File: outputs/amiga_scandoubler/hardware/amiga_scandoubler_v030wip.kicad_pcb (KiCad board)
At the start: 4 copper layers, 95 x 95 mm, 135 parts, among them J1 33DSMT1-E15SNCT, J2 33DSMT1-E15SNCT, J3 TYPE-C-31-M-12, J4 JTAG 2x05 2.54mm, U1 TVP7002PZP, U2 GW1N-LV4QN88C6/I5, U3 ADV7125KSTZ140, U4 SN74LVC2G17DBVR, U5 SN74LVC2G17DBVR, U6 SN74LVC1G17DBVR, U7 TPS62160DSGR, U8 TPS62160DSGR, U9 TPS62160DSGR, Y1 27MHz ECS-3225MVLC

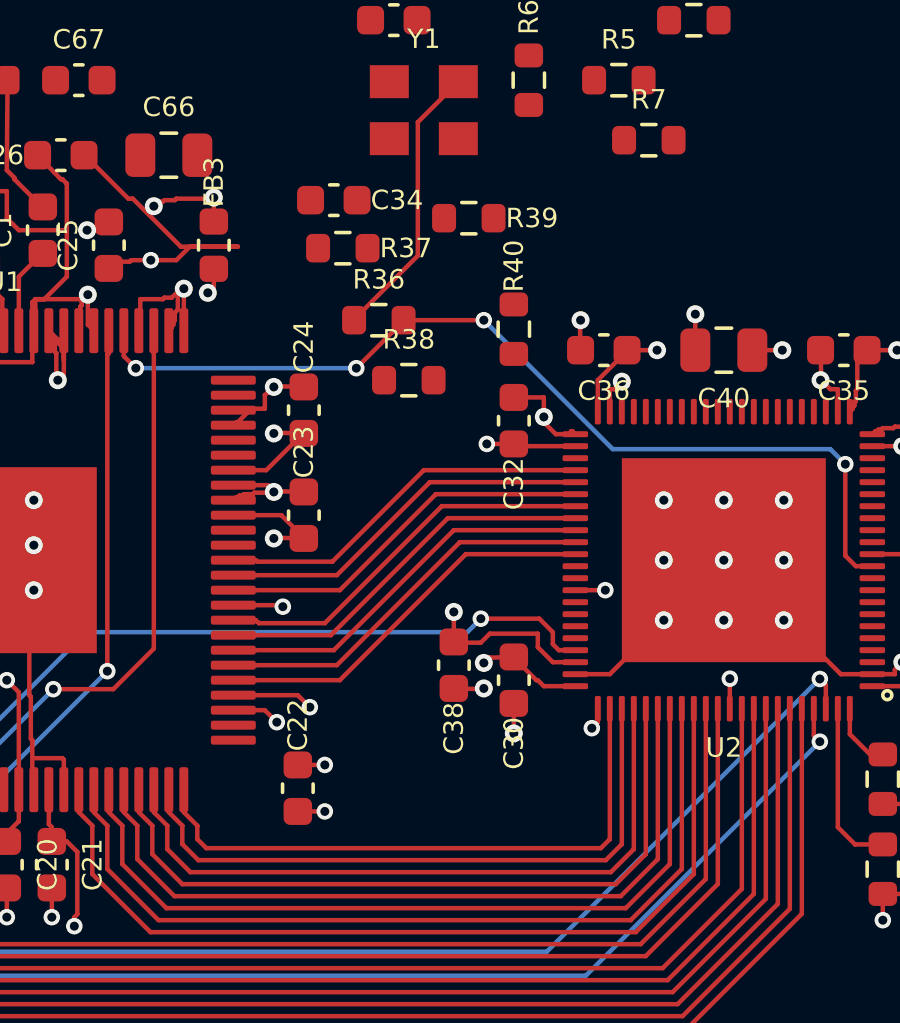
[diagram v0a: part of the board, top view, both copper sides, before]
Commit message: v030wip: C34(U2 3V3 パスコン)の孤立を解消
- C34 を (37,30) から U2 左下角 (45.4,49.15, 270°) へ移動
- pad1(3V3) を U2.67 の既存 3V3 ビアへ接続、pad2(GND) に GND ビアを追加
- U2 左の制御線予約領域と B.Cu 通路は回避
- KiCad 7 DRC: エラー 0、未接続 112→110 (3V3/GND 各 -1 のみ)
- 電源監査: 電源 75・GND 80 件 PASS。残る FAIL は U2 再ピン由来(課題5/9)
- CLAUDE.md と revision_0.30wip.md を更新、配置スクリプトを追加

Co-Authored-By: Claude Opus 5.5 <noreply@anthropic.com>
Claude-Session: https://claude.ai/code/session_019f929sAJ7LRnJRRFvA6g9F
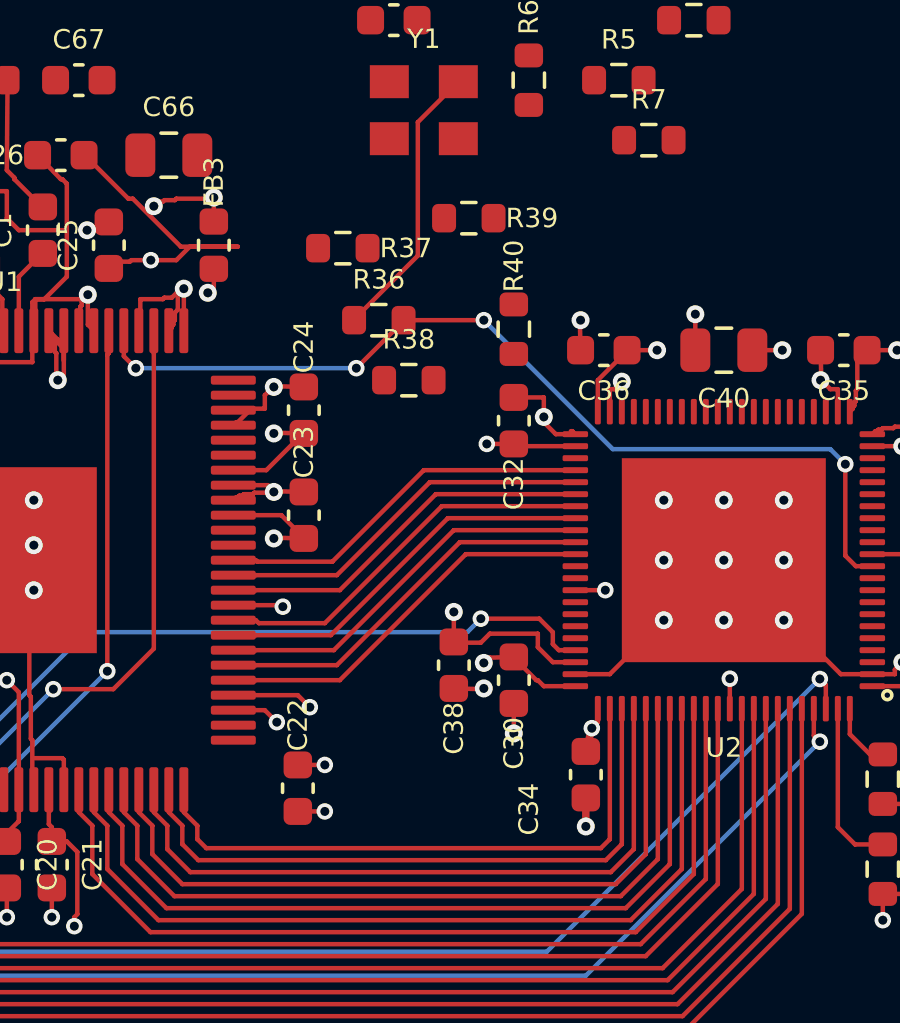
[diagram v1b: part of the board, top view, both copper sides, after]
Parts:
- moved C34 20.9 mm to (45.4, 49.1), turned to -90 degrees
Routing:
- net GND: track 349.1 -> 350.0 mm, vias 102 -> 103
- net 3V3: track 77.3 -> 78.1 mm
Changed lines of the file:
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@@
   )
   (footprint "Capacitor_SMD:C_0603_1608Metric" (layer "F.Cu")
-    (at 37 30)
+    (at 45.4 49.15 -90)
     (descr "Capacitor SMD 0603 (1608 Metric), square (rectangular) end terminal, IPC_7351 nominal, (Body size source: IPC-SM-782 page 76, https://www.pcb-3d.com/wordpress/wp-content/uploads/ipc-sm-782a_amendment_1_and_2.pdf), generated with kicad-footprint-generator")
     (tags "capacitor")
     (attr smd)
-    (fp_text reference "C34" (at 2.105001 0) (layer "F.SilkS")
+    (fp_text reference "C34" (at 1.15 1.9 -90) (layer "F.SilkS")
         (effects (font (size 0.65 0.65) (thickness 0.1)))
     )
-    (fp_text value "100nF" (at 0 1.43) (layer "F.Fab") hide
+    (fp_text value "100nF" (at 0 1.43 -90) (layer "F.Fab") hide
         (effects (font (size 1 1) (thickness 0.15)))
     )
-    (fp_text user "${REFERENCE}" (at 0 0) (layer "F.Fab")
+    (fp_text user "${REFERENCE}" (at 0 0 -90) (layer "F.Fab")
         (effects (font (size 0.4 0.4) (thickness 0.06)))
     )
@@
     (fp_line (start 0.8 0.4) (end -0.8 0.4)
       (stroke (width 0.1) (type solid)) (layer "F.Fab"))
-    (pad "1" smd roundrect (at -0.775 0) (size 0.9 0.95) (layers "F.Cu" "F.Paste" "F.Mask") (roundrect_rratio 0.25)
+    (pad "1" smd roundrect (at -0.775 0 270) (size 0.9 0.95) (layers "F.Cu" "F.Paste" "F.Mask") (roundrect_rratio 0.25)
       (net 54 "3V3"))
-    (pad "2" smd roundrect (at 0.775 0) (size 0.9 0.95) (layers "F.Cu" "F.Paste" "F.Mask") (roundrect_rratio 0.25)
+    (pad "2" smd roundrect (at 0.775 0 270) (size 0.9 0.95) (layers "F.Cu" "F.Paste" "F.Mask") (roundrect_rratio 0.25)
       (net 43 "GND"))
     (model "${KICAD6_3DMODEL_DIR}/Capacitor_SMD.3dshapes/C_0603_1608Metric.wrl"
@@
   (segment (start 75.4 37.55) (end 75.45 37.5) (width 0.15) (layer "F.Cu") (net 43))
   (segment (start 43 47.8) (end 43 47.775) (width 0.15) (layer "F.Cu") (net 43))
+  (segment (start 45.4 49.925) (end 45.4 50.875) (width 0.25) (layer "F.Cu") (net 43))
   (segment (start 16 40.225) (end 15.2 40.2) (width 0.15) (layer "F.Cu") (net 43))
   (segment (start 45.05 38.2) (end 43.3 38.2) (width 0.15) (layer "F.Cu") (net 43))
@@
   (via (at 16.95 36.8) (size 0.6) (drill 0.3) (layers "F.Cu" "B.Cu") (net 43))
   (via (at 28.8 33.15) (size 0.6) (drill 0.3) (layers "F.Cu" "B.Cu") (net 43))
+  (via (at 45.4 50.875) (size 0.6) (drill 0.3) (layers "F.Cu" "B.Cu") (net 43))
   (via (at 68.6375 44.95) (size 0.6) (drill 0.3) (layers "F.Cu" "B.Cu") (net 43))
   (via (at 15 40.425) (size 0.6) (drill 0.3) (layers "F.Cu" "B.Cu") (net 43))
@@
   (segment (start 27.6 50.9) (end 27.6 51.375) (width 0.15) (layer "F.Cu") (net 54))
   (segment (start 28.45 51.725) (end 28.45 53.8) (width 0.15) (layer "F.Cu") (net 54))
+  (segment (start 45.4 48.375) (end 45.6 47.6) (width 0.25) (layer "F.Cu") (net 54))
   (segment (start 54.35 36.85) (end 54.35 36.75) (width 0.15) (layer "F.Cu") (net 54))
   (segment (start 54.95 41.8) (end 56.45 41.8) (width 0.15) (layer "F.Cu") (net 54))

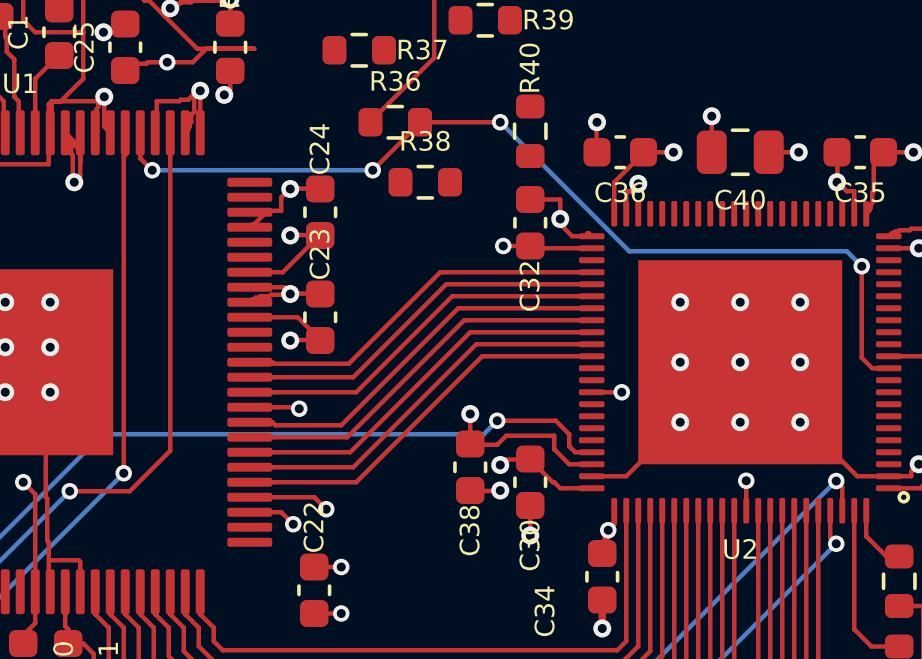
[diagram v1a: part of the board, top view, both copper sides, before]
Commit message: v030wip: 課題2 U2 左の制御線(SDA/SCL/RESET/PWDN)の本線を配線
- U1 内周ビア → B.Cu → U2 前面ビアで 4 本を接続(交差なし、各ビア2個)
  x=35 のビア列の隙間を上帯 SDA/SCL、下帯 RESET/PWDN で通過
- ADC_CLK の B.Cu 終点を (43.95,45.0) へ移し U2.60/61 の引き出し通路を確保
- U2.64 3V3 を内周ビアへ、U2.65 GND スタブを短縮
- KiCad 7 DRC: エラー 0、未接続 110→106(4ネット各 -1)。導通確認済み
- 電源監査: 電源 75・GND 80 PASS
- プルアップ R37–R40 は 0603 では収まらず未接続(判断待ち)
- KiCad 7 用編集ヘルパ pcbk7.py、配置探索 pullsearch.py、再現スクリプトを追加

Co-Authored-By: Claude Opus 5.5 <noreply@anthropic.com>
Claude-Session: https://claude.ai/code/session_019f929sAJ7LRnJRRFvA6g9F
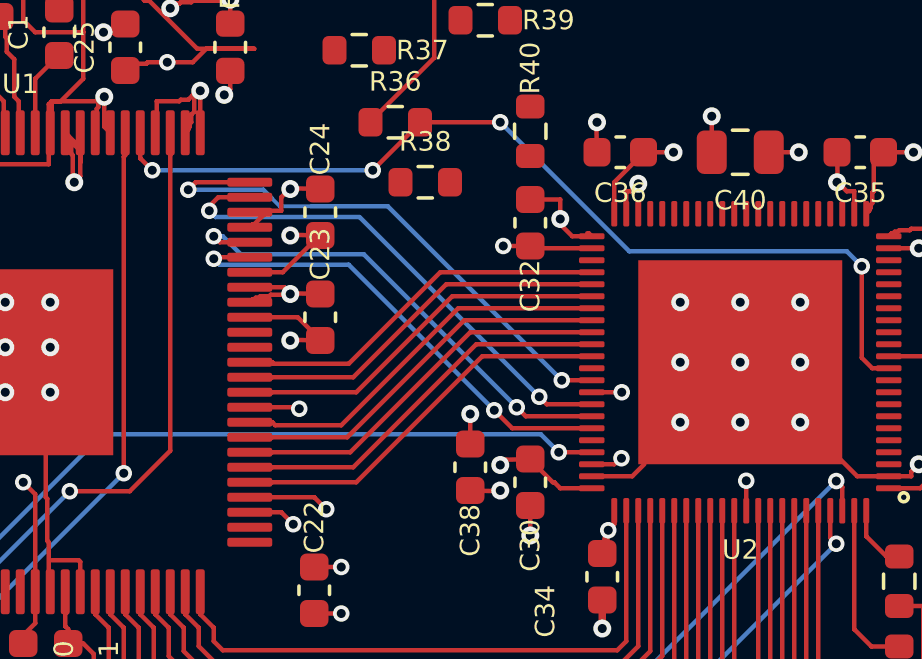
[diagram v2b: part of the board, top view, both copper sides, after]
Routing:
- net I2C_SDA: track 0.00 -> 18.2 mm, vias 0 -> 2
- net I2C_SCL: track 0.00 -> 17.0 mm, vias 0 -> 2
- net ADC_RESET_N: track 0.00 -> 16.4 mm, vias 0 -> 2
- net ADC_PWDN: track 0.00 -> 16.2 mm, vias 0 -> 2
- net GND: track 350.0 -> 345.4 mm
- net 3V3: track 78.1 -> 74.3 mm, vias 26 -> 27
- net ADC_CLK: track 28.9 -> 28.3 mm

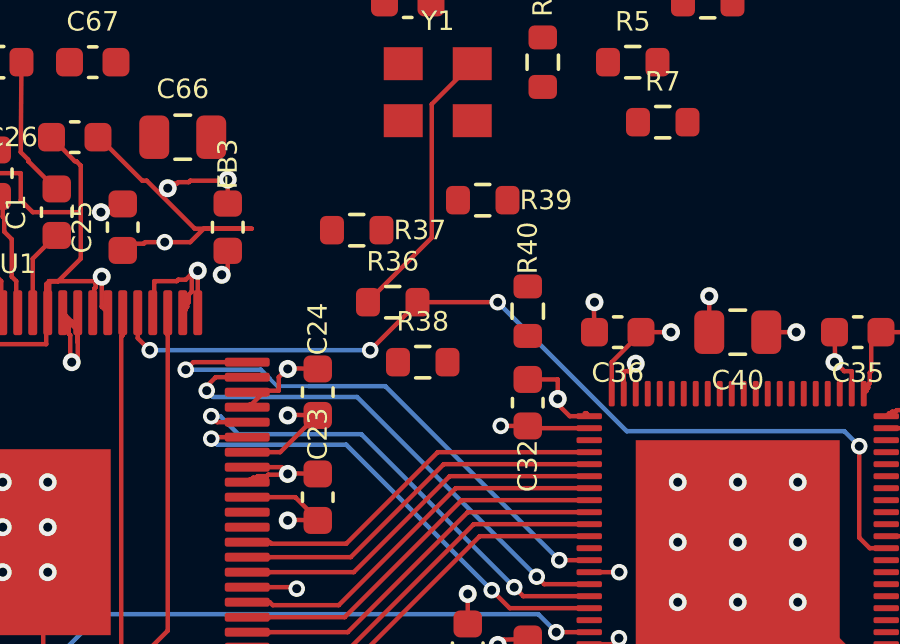
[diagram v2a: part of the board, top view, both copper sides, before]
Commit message: v030wip: R37–R40 を 0402 化してプルアップ／プルダウンを接続(課題2完了)
- 0603 では空き領域に収まらないため、利用者判断で R_0402_1005Metric に変更
- 4 本を縦置き 0.95mm ピッチで配置し、信号ビアを各 B.Cu 配線上へ
- 3V3/GND は面へのビア(R37 は R38 の 3V3 ビアを共用)
- 回路図・ネットリスト・circuit_manifest のフットプリント欄を更新
- KiCad 7 DRC: エラー 0、未接続 106→98。導通確認済み、電源監査 PASS

Co-Authored-By: Claude Opus 5.5 <noreply@anthropic.com>
Claude-Session: https://claude.ai/code/session_019f929sAJ7LRnJRRFvA6g9F
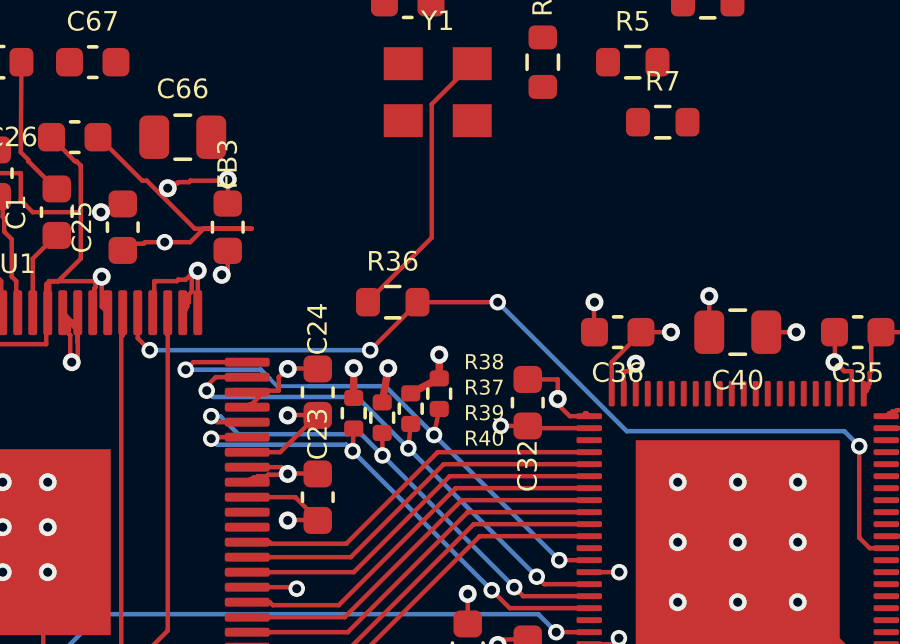
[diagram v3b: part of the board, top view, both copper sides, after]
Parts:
- R37, R38, R39, R40: footprint Resistor_SMD:R_0603_1608Metric -> R_0402_1005Metric
- moved R39 7.99 mm to (38.1, 37.9), turned to 90 degrees
- moved R40 6.72 mm to (37.2, 37.7)
- moved R37 6.22 mm to (39.1, 37.5), turned to 90 degrees
- moved R38 1.19 mm to (40.0, 37.0), turned to 90 degrees
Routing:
- net 3V3: track 74.3 -> 77.2 mm, vias 27 -> 29
- net GND: track 345.4 -> 346.6 mm, vias 103 -> 104
- net I2C_SDA: track 18.2 -> 19.1 mm, vias 2 -> 3
- net I2C_SCL: track 17.0 -> 17.9 mm, vias 2 -> 3
- net ADC_PWDN: track 16.2 -> 16.9 mm, vias 2 -> 3
- net ADC_RESET_N: track 16.4 -> 17.1 mm, vias 2 -> 3

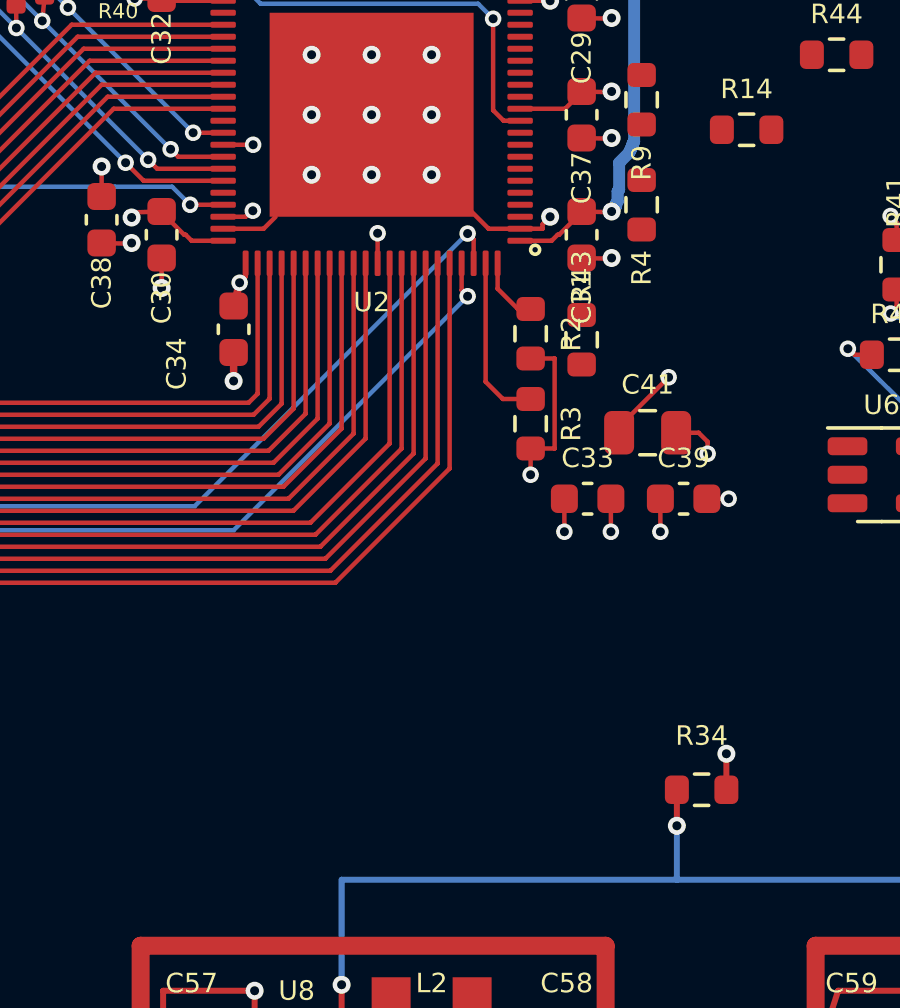
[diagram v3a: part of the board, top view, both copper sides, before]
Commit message: v030wip: 課題3 POWER_GOOD(U2.62)を既存の南側配線へ接続
- U2.62 → 内周ビア (46.04,44.45) → B.Cu で EP 下 y=44.65 を東へ
  → 45° で南東 → x=59.075 を南下 → 既存ビア (60.175,65.7)
- y=41 の通路は課題4(PSAVE)用に予約して回避
- KiCad 7 DRC: エラー 0、未接続 98→97(POWER_GOOD のみ)
- U8.8/U9.8/R34.1 との導通確認、電源監査 PASS

Co-Authored-By: Claude Opus 5.5 <noreply@anthropic.com>
Claude-Session: https://claude.ai/code/session_019f929sAJ7LRnJRRFvA6g9F
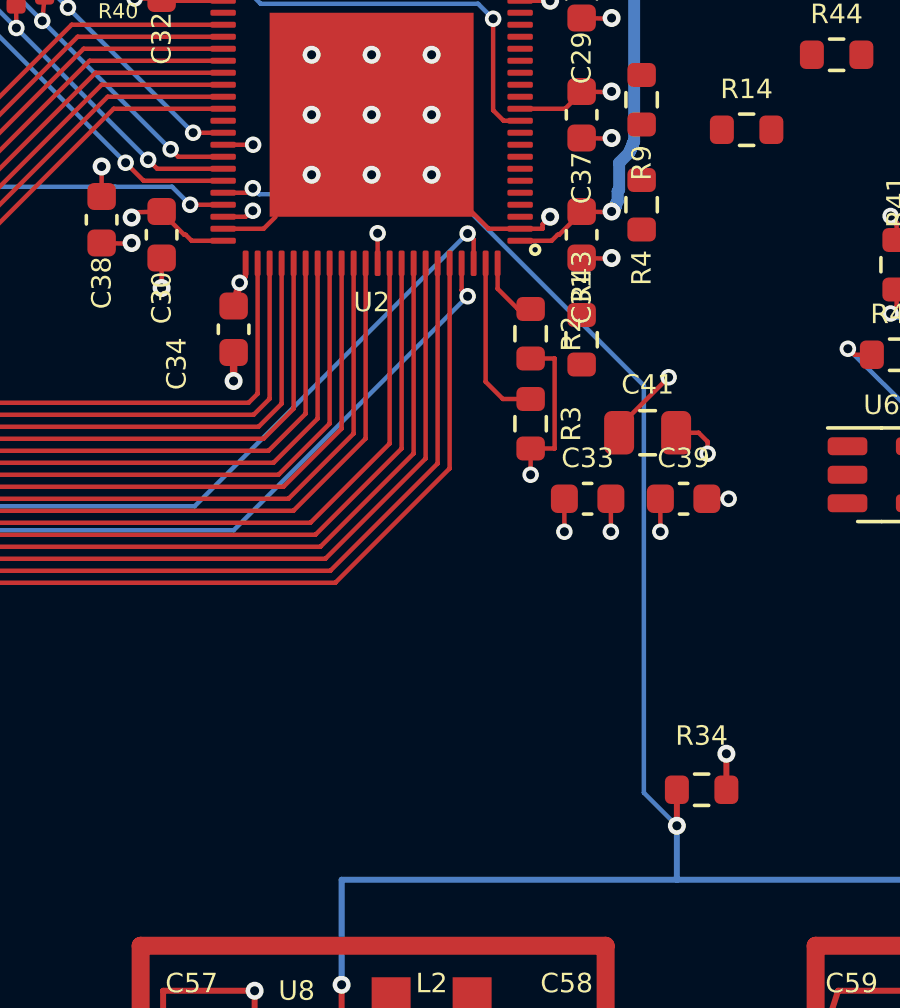
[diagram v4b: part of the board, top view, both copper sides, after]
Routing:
- net POWER_GOOD: track 36.1 -> 68.0 mm, vias 3 -> 4
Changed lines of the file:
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@@
   (segment (start 65.875 49.8) (end 67.7 51.6) (width 0.15) (layer "B.Cu") (net 63))
   (segment (start 65.9 49.8) (end 65.875 49.8) (width 0.15) (layer "B.Cu") (net 63))
+  (segment (start 45.89 44.6) (end 46.04 44.45) (width 0.15) (layer "F.Cu") (net 64))
+  (segment (start 45.05 44.6) (end 45.89 44.6) (width 0.15) (layer "F.Cu") (net 64))
   (segment (start 71.5 72.25) (end 71.5 71) (width 0.2) (layer "F.Cu") (net 64))
   (segment (start 70.95 72.25) (end 71.5 72.25) (width 0.2) (layer "F.Cu") (net 64))
@@
   (segment (start 48.45 72.25) (end 49 72.25) (width 0.2) (layer "F.Cu") (net 64))
   (via (at 60.175 65.7) (size 0.6) (drill 0.3) (layers "F.Cu" "B.Cu") (net 64))
+  (via (at 46.04 44.45) (size 0.55) (drill 0.3) (layers "F.Cu" "B.Cu") (net 64))
   (via (at 49 71) (size 0.6) (drill 0.3) (layers "F.Cu" "B.Cu") (net 64))
   (via (at 71.5 71) (size 0.6) (drill 0.3) (layers "F.Cu" "B.Cu") (net 64))
   (segment (start 49 67.5) (end 71.5 67.5) (width 0.2) (layer "B.Cu") (net 64))
+  (segment (start 46.04 44.45) (end 46.25 44.65) (width 0.15) (layer "B.Cu") (net 64))
+  (segment (start 52.7 44.65) (end 59.075 51.025) (width 0.15) (layer "B.Cu") (net 64))
+  (segment (start 59.075 64.599999) (end 60.175 65.7) (width 0.15) (layer "B.Cu") (net 64))
+  (segment (start 59.075 51.025) (end 59.075 64.599999) (width 0.15) (layer "B.Cu") (net 64))
+  (segment (start 46.25 44.65) (end 52.7 44.65) (width 0.15) (layer "B.Cu") (net 64))
   (segment (start 49 71) (end 49 67.5) (width 0.2) (layer "B.Cu") (net 64))
   (segment (start 60.175 65.7) (end 60.175 67.5) (width 0.2) (layer "B.Cu") (net 64))
